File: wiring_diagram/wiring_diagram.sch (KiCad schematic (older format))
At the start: 27 parts

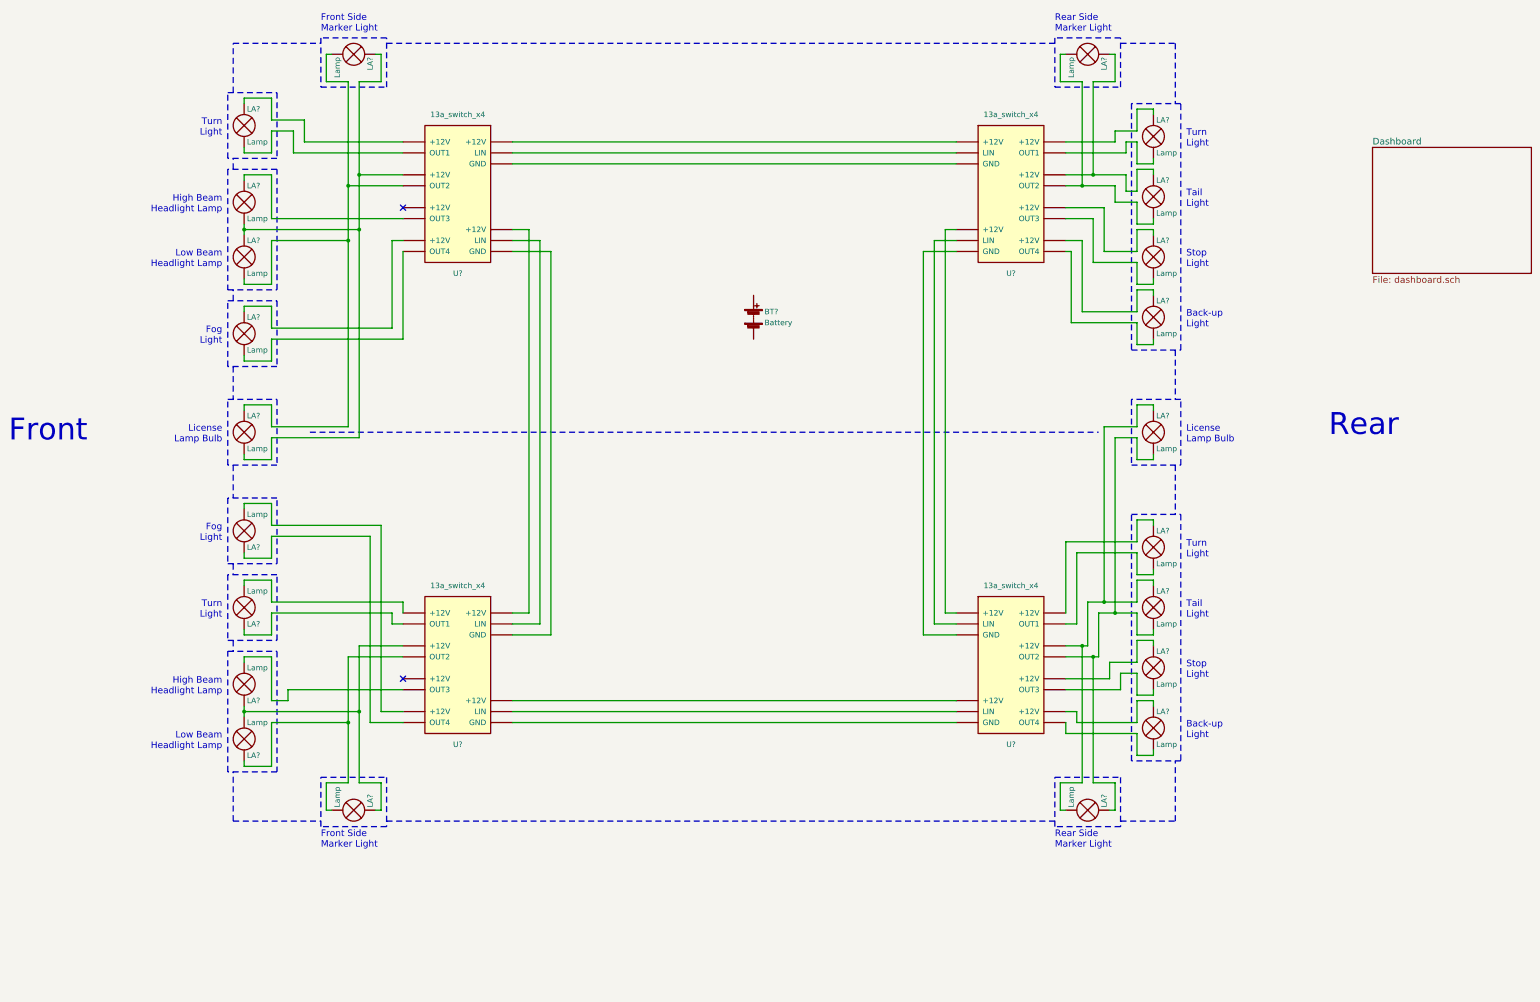
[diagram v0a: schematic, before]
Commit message: updated wiring diagram
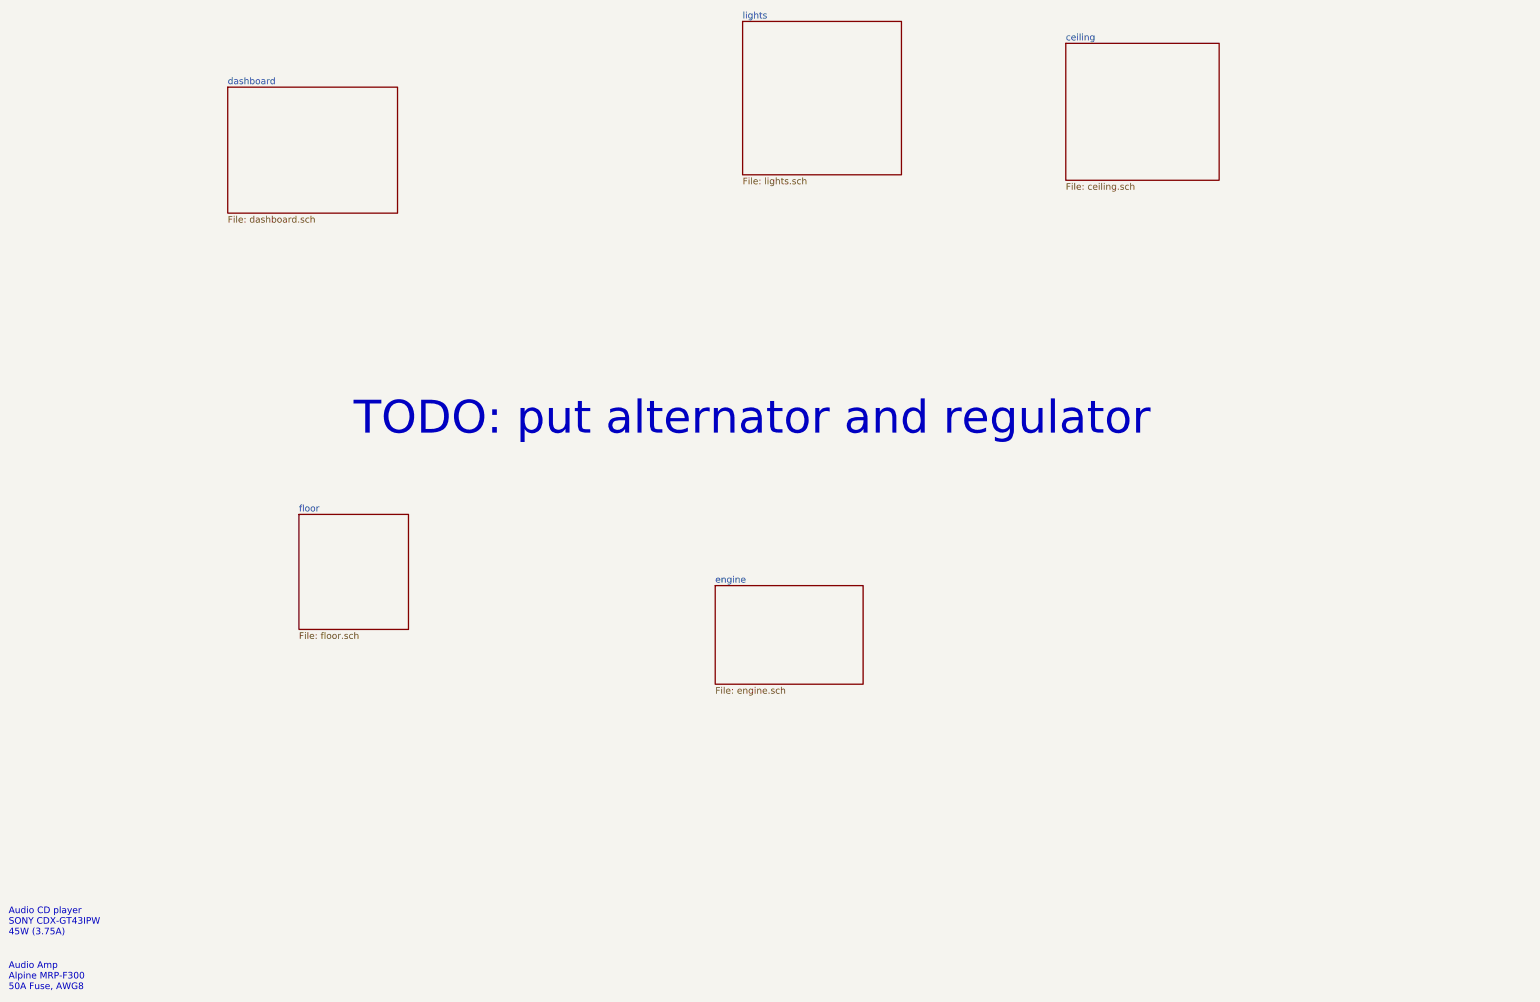
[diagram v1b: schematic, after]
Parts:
- removed BT?: Battery, symbol Battery
- removed LA? (x22): Lamp, symbol Lamp
- removed U? (x4): 13a_switch_x4, symbol 13a_switch_x4
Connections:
- no-connect marks 2 -> 0
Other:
- note added: "Audio Amp\nAlpine MRP-F300\n50A Fuse, AWG8"
- note added: "Audio CD player\nSONY CDX-GT43IPW\n45W (3.75A)"
- note added: "TODO: put alternator and regulator"
- note removed: "Back-up\nLight"
- note removed: "Fog\nLight"
- note removed: "Front"
- note removed: "Front Side\nMarker Light"
- note removed: "High Beam\nHeadlight Lamp"
- note removed: "License\nLamp Bulb"
- note removed: "Low Beam\nHeadlight Lamp"
- note removed: "Rear"
- note removed: "Rear Side\nMarker Light"
- note removed: "Stop\nLight"
- note removed: "Tail\nLight"
- note removed: "Turn\nLight"

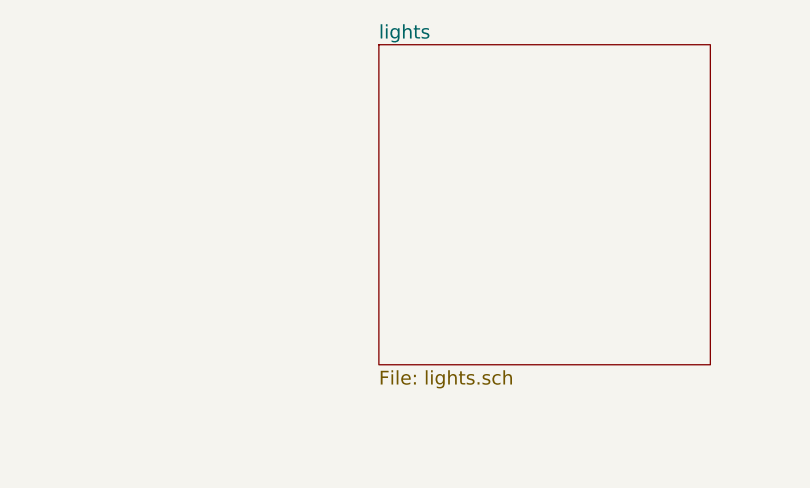
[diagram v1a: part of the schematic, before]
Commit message: Adding fuel pump driver
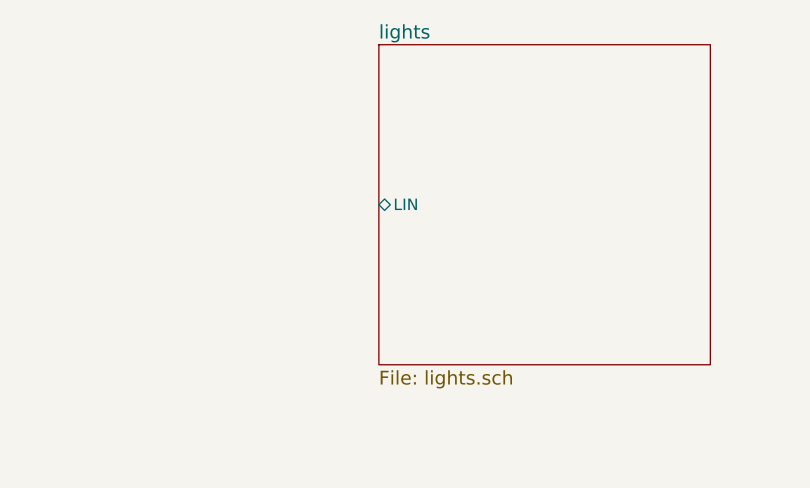
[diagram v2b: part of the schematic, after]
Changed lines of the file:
@@
-EESchema Schematic File Version 2
-LIBS:power
-LIBS:device
-LIBS:transistors
-LIBS:conn
-LIBS:linear
-LIBS:regul
-LIBS:74xx
-LIBS:cmos4000
-LIBS:adc-dac
-LIBS:memory
-LIBS:xilinx
-LIBS:microcontrollers
-LIBS:dsp
-LIBS:microchip
-LIBS:analog_switches
-LIBS:motorola
-LIBS:texas
-LIBS:intel
-LIBS:audio
-LIBS:interface
-LIBS:digital-audio
-LIBS:philips
-LIBS:display
-LIBS:cypress
-LIBS:siliconi
-LIBS:opto
-LIBS:atmel
-LIBS:contrib
-LIBS:valves
-LIBS:13a_switch_x4
-LIBS:switches
-LIBS:motors
-LIBS:inputs_x8
-LIBS:lin
-LIBS:sw_sp4t
-LIBS:tdc_marker_unit
+EESchema Schematic File Version 4
 LIBS:wiring_diagram-cache
-EELAYER 25 0
+EELAYER 26 0
 EELAYER END
 $Descr A3 16535 11693
@@
 F0 "lights" 60
 F1 "lights.sch" 60
+F2 "LIN" B L 8250 2400 50
 $EndSheet
 $Sheet
